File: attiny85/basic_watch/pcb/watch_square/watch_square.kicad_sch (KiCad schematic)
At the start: 22 parts, among them J2 USB C, J3 Programmer, P1 JST_LIPO, SW1 Wake, SW2 Select, SW3 Set, SW4 Reset, U1 ATTINY85, U2 MCP73831-2-OT, U3 SSD1306_OLED_Display_128x64

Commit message: Round watch footprint cannot accomodate all components
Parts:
- BT1: value Battery_Cell -> BT1
- J2: renamed from J3; value Programmer -> PROG
- OLED_DISPLAY1: renamed from U3; value SSD1306_OLED_Display_128x64 -> OLED DISPLAY
- P1: value JST_LIPO -> LIPO B2
- RST1: renamed from SW4; value Reset -> RST
- SEL1: renamed from SW2; value Select -> SEL
- SET1: renamed from SW3; value Set -> SET
- WK1: renamed from SW1; value Wake -> WK
- renumbered U1 to ATTINY1, H4 to H2, H2 to H3, H3 to H4, J2 to J1, R3 to R1, R4 to R2, R1 to R3, R2 to R4, U2 to U1
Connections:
- net GND: now also J2.S1 (SHIELD), J2.S2 (SHIELD), OLED_DISPLAY1.4 (SDA); no longer OLED_DISPLAY1.1 (GND)
- net MOSI: now also OLED_DISPLAY1.1 (GND); no longer OLED_DISPLAY1.4 (SDA)
- net SCK: now also OLED_DISPLAY1.2 (VCC); no longer OLED_DISPLAY1.3 (SCK)
- net VCC: now also OLED_DISPLAY1.3 (SCK); no longer OLED_DISPLAY1.2 (VCC)
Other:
- moved on the sheet: C1, C2, J2, LED1, R1, R2, U1

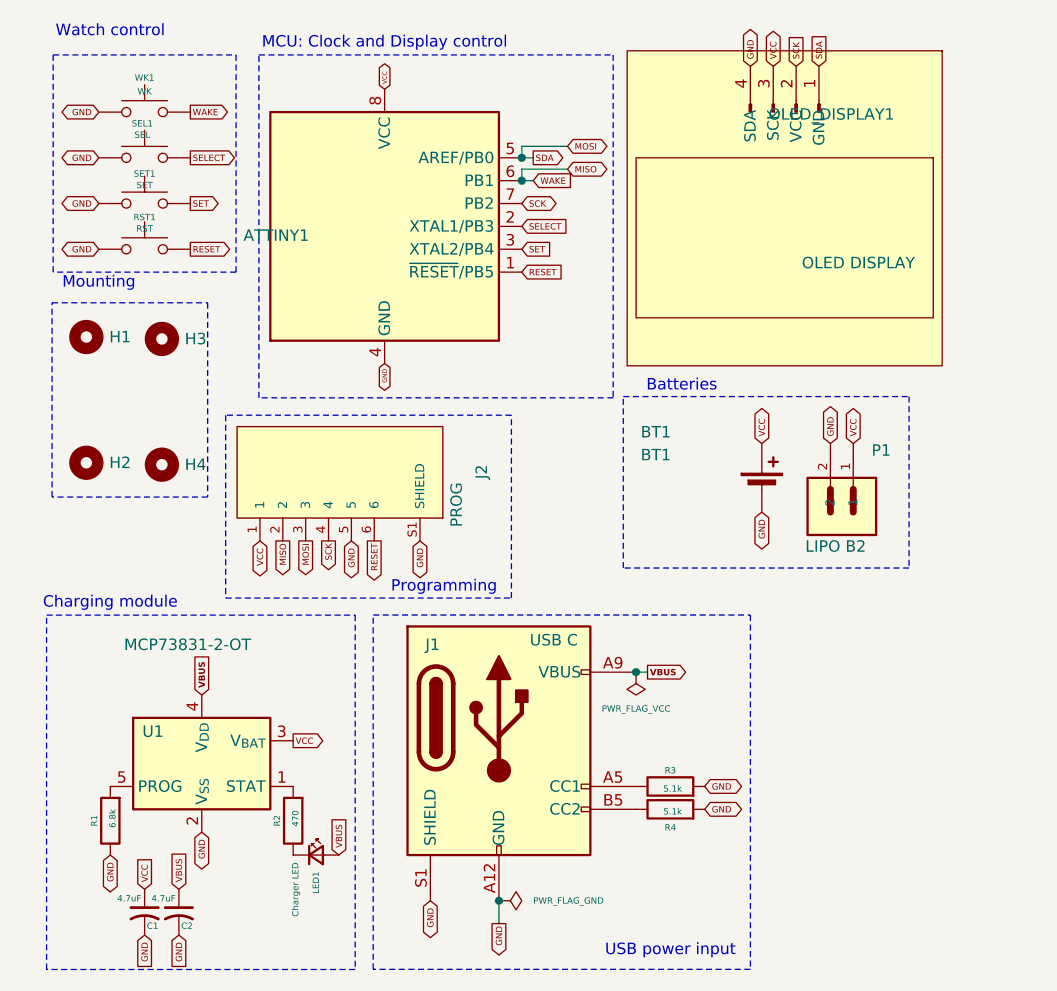
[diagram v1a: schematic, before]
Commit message: changed footprints
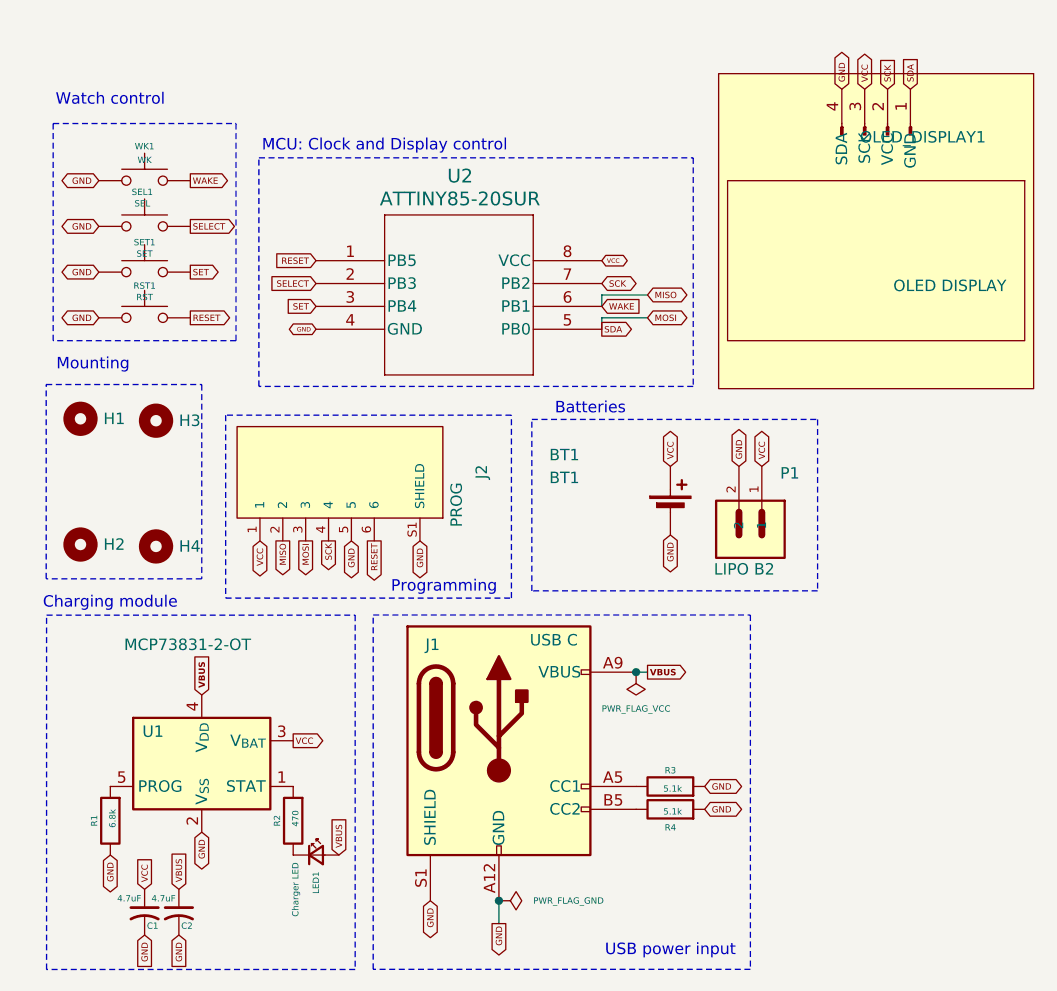
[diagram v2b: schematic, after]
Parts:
- removed ATTINY1: ATTINY85, Package_DIP:DIP-8_W7.62mm_SMDSocket_SmallPads, symbol MCU_Microchip_ATtiny:ATtiny85-20P
- added U2: ATTINY85-20SUR, My_ATTINY:8S2_ATM-L, symbol My_Symbols:ATTINY85-20SUR
- BT1: LCSC (none) -> C238069
- C1, C2: LCSC (none) -> C380343
- J1: LCSC (none) -> C7507406
- J2: LCSC (none) -> C265405
- LED1: LCSC (none) -> C19171391
- P1: LCSC (none) -> C295747
- R1: LCSC (none) -> C2907338
- R2: LCSC (none) -> C2907329
- R3, R4: LCSC (none) -> C2930296
- RST1, SEL1, SET1, WK1: LCSC (none) -> C2689642; MFR part (none) -> PTS636SK25SMTRLFS
- U1: LCSC (none) -> C424093
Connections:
- net GND: now also U2.4 (GND)
- net MISO: now also U2.6 (PB1)
- net MOSI: now also U2.5 (PB0)
- net RESET: now also U2.1 (PB5)
- net SCK: now also U2.7 (PB2)
- net SELECT: now also U2.2 (PB3)
- net SET: now also U2.3 (PB4)
- net VCC: now also U2.8 (VCC)
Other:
- moved on the sheet: BT1, H1, H2, H3, H4, OLED_DISPLAY1, P1, RST1, SEL1, SET1, WK1

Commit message: corrected OLED orientation
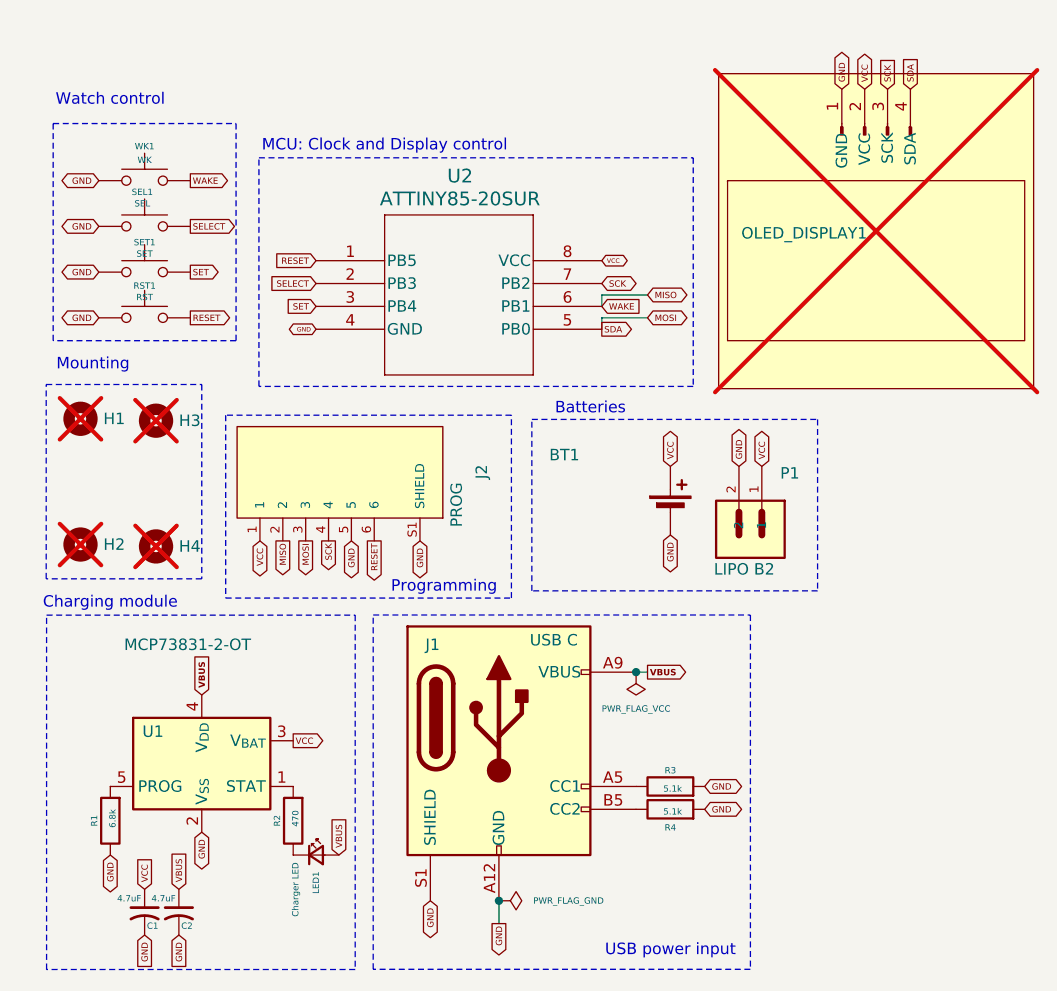
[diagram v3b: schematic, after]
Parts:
- BT1, U1, U2: Rotation Offset (none) -> -90
- H1, H2, H3, H4: now not fitted
- J1: Position Offset (none) -> 0,1.143
- J2: Position Offset (none) -> 0,-2.9845; Rotation Offset (none) -> 180
- OLED_DISPLAY1: now not fitted; now left out of the parts list
- P1: Position Offset (none) -> 0,2.8575; Rotation Offset (none) -> 180
- R1: LCSC C2907338 -> C17772
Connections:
- net GND: now also OLED_DISPLAY1.1 (GND); no longer OLED_DISPLAY1.4 (SDA)
- net MOSI: now also OLED_DISPLAY1.4 (SDA); no longer OLED_DISPLAY1.1 (GND)
- net SCK: now also OLED_DISPLAY1.3 (SCK); no longer OLED_DISPLAY1.2 (VCC)
- net VCC: now also OLED_DISPLAY1.2 (VCC); no longer OLED_DISPLAY1.3 (SCK)
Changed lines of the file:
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@@
+			)
+		)
+		(property "Rotation Offset" "180"
+			(at 132.196 108.6077 0)
+			(effects
+				(font
+					(size 1.27 1.27)
+				)
+				(hide yes)
+			)
+		)
+		(property "Position Offset" "0,-2.9845"
+			(at 132.196 108.6077 0)
+			(effects
+				(font
+					(size 1.27 1.27)
+				)
+				(hide yes)
 			)
 		)
@@
 			)
 		)
+		(property "Rotation Offset" "180"
+			(at 179.07 113.03 90)
+			(effects
+				(font
+					(size 1.27 1.27)
+				)
+				(hide yes)
+			)
+		)
+		(property "Position Offset" "0,2.8575"
+			(at 179.07 113.03 90)
+			(effects
+				(font
+					(size 1.27 1.27)
+				)
+				(hide yes)
+			)
+		)
 		(pin "1"
 		)
@@
 		(in_bom no)
 		(on_board yes)
-		(dnp no)
+		(dnp yes)
 		(fields_autoplaced yes)
 		(property "Reference" "H2"
@@
 			)
 		)
+		(property "LCSC" ""
+			(at 104.6366 116.629 0)
+			(effects
+				(font
+					(size 1.27 1.27)
+				)
+			)
+		)
 		(instances
 			(project "watch"
@@
 		(lib_id "My_Symbols:SSD1306_OLED_Display_128x64")
 		(at 193.04 67.31 0)
-		(mirror y)
-		(unit 1)
-		(exclude_from_sim no)
-		(in_bom yes)
-		(on_board yes)
-		(dnp no)
+		(unit 1)
+		(exclude_from_sim no)
+		(in_bom no)
+		(on_board yes)
+		(dnp yes)
 		(property "Reference" "OLED_DISPLAY1"
-			(at 205.232 71.374 0)
+			(at 178.054 82.042 0)
 			(effects
 				(font
@@
 		)
 		(property "Value" "OLED DISPLAY"
-			(at 207.518 87.884 0)
-			(effects
-				(font
-					(size 1.27 1.27)
-				)
-				(justify left)
+			(at 181.102 88.646 0)
+			(effects
+				(font
+					(size 1.27 1.27)
+				)
+				(justify left)
+				(hide yes)
 			)
 		)
@@
 		)
 		(property "Datasheet" ""
-			(at 191.135 70.485 90)
+			(at 194.945 70.485 90)
 			(effects
 				(font
@@
 		)
 		(property "Description" "SSD1306 OLED Display with pins"
-			(at 192.024 58.674 0)
-			(effects
-				(font
-					(size 1.27 1.27)
-				)
-				(hide yes)
+			(at 194.056 58.674 0)
+			(effects
+				(font
+					(size 1.27 1.27)
+				)
+				(hide yes)
+			)
+		)
+		(property "LCSC" ""
+			(at 193.04 67.31 0)
+			(effects
+				(font
+					(size 1.27 1.27)
+				)
 			)
 		)
@@
 		(in_bom no)
 		(on_board yes)
-		(dnp no)
+		(dnp yes)
 		(fields_autoplaced yes)
 		(property "Reference" "H3"
@@
 			)
 		)
+		(property "LCSC" ""
+			(at 113.03 102.87 0)
+			(effects
+				(font
+					(size 1.27 1.27)
+				)
+			)
+		)
 		(instances
 			(project "watch"
@@
 			)
 		)
+		(property "Rotation Offset" "-90"
+			(at 118.11 140.97 0)
+			(effects
+				(font
+					(size 1.27 1.27)
+				)
+				(hide yes)
+			)
+		)
 		(pin "2"
 		)
@@
 			)
 		)
-		(property "LCSC" "C2907338"
+		(property "LCSC" "C17772"
 			(at 107.95 147.32 0)
 			(effects
@@
 			)
 		)
+		(property "Rotation Offset" "-90"
+			(at -50.8 85.09 0)
+			(effects
+				(font
+					(size 1.27 1.27)
+				)
+				(hide yes)
+			)
+		)
 		(pin "1"
 		)
@@
 		(in_bom no)
 		(on_board yes)
-		(dnp no)
+		(dnp yes)
 		(fields_autoplaced yes)
 		(property "Reference" "H1"
@@
 			)
 		)
+		(property "LCSC" ""
+			(at 104.6366 102.659 0)
+			(effects
+				(font
+					(size 1.27 1.27)
+				)
+			)
+		)
 		(instances
 			(project ""
@@
 		(in_bom no)
 		(on_board yes)
-		(dnp no)
+		(dnp yes)
 		(fields_autoplaced yes)
 		(property "Reference" "H4"
@@
 			)
 		)
+		(property "LCSC" ""
+			(at 113.03 116.84 0)
+			(effects
+				(font
+					(size 1.27 1.27)
+				)
+			)
+		)
 		(instances
 			(project "watch"
@@
 		)
 		(property "LCSC" "C7507406"
+			(at 151.13 138.43 0)
+			(effects
+				(font
+					(size 1.27 1.27)
+				)
+				(hide yes)
+			)
+		)
+		(property "Position Offset" "0,1.143"
 			(at 151.13 138.43 0)
 			(effects
@@
 				)
 				(justify left)
+				(hide yes)
 			)
 		)
@@
 			(at 170.18 113.03 0)
 			(effects
+				(font
+					(size 1.27 1.27)
+				)
+				(hide yes)
+			)
+		)
+		(property "Rotation Offset" "-90"
+			(at 170.18 113.03 0)
+			(effects
